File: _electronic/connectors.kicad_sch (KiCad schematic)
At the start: 7 parts

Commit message: BETA first upload
nothing major done here:
* updated KiCAD files to v9
* removed alternative 6v feed-in. The proposed buck converter is fine.
* added to all components LCSC component IDs. With this, exporting the project as gerber files also automatically creates correct BOM for JLCPCB manufacturing
*
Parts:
- J_HALL1, J_SERVO1: LCSC (none) -> C2937625
- J_LEDE1, J_LEDP1: LCSC (none) -> C492401
- J_OLED1: LCSC (none) -> C32713263
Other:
- title: E-TKT v1.0 -> E-TKT v2.0 BETA

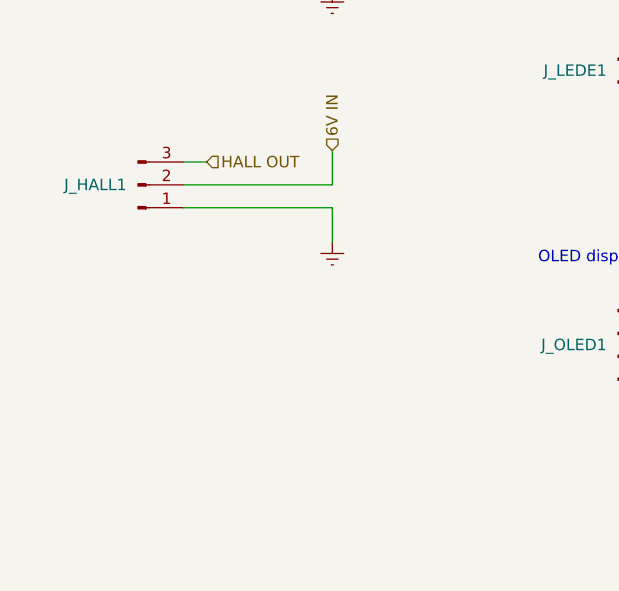
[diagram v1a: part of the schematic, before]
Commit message: Added endstop
added footprint for a microswitch with roller as enstop. updated the CAD correspondingly by adding M4 hole in the nema wheel hub for an M4 12mm/16mm set screw (the ones with a pointy end).
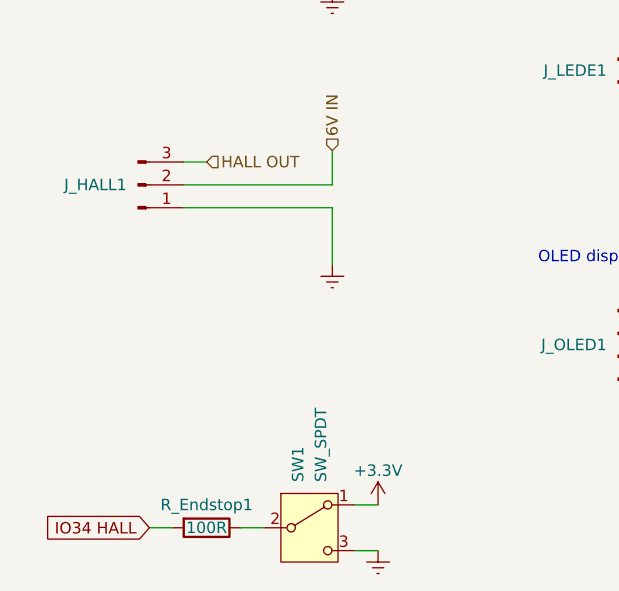
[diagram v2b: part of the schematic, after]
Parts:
- added R_Endstop1: 100R, Resistor_SMD:R_0603_1608Metric_Pad0.98x0.95mm_HandSolder, symbol Device:R
- added SW1: SW_SPDT, EASYEDA2KICAD:SW-TH_JL010, symbol Switch:SW_SPDT
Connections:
- net GNDREF: now also SW1.3 (C)
- new net: R_Endstop1.1, SW1.2 (B)
- new net +3.3V: SW1.1 (A)
- new net IO34 HALL: R_Endstop1.2

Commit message: sturdyfy E-TKT
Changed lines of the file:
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@@
 	(wire
 		(pts
-			(xy 135.89 154.94) (xy 138.43 154.94)
+			(xy 135.89 154.94) (xy 152.4 154.94)
 		)
 		(stroke
@@
 	(wire
 		(pts
-			(xy 135.89 149.86) (xy 138.43 149.86)
+			(xy 135.89 149.86) (xy 152.4 149.86)
 		)
 		(stroke
@@
 	(symbol
 		(lib_id "power:+3.3V")
-		(at 138.43 149.86 0)
+		(at 152.4 149.86 0)
 		(unit 1)
 		(exclude_from_sim no)
@@
 		(dnp no)
 		(property "Reference" "#PWR06"
-			(at 138.43 153.67 0)
+			(at 152.4 153.67 0)
 			(effects
 				(font
@@
 		)
 		(property "Value" "+3.3V"
-			(at 138.43 146.05 0)
+			(at 152.4 146.05 0)
 			(effects
 				(font
@@
 		)
 		(property "Footprint" ""
-			(at 138.43 149.86 0)
+			(at 152.4 149.86 0)
 			(effects
 				(font
@@
 		)
 		(property "Datasheet" ""
-			(at 138.43 149.86 0)
+			(at 152.4 149.86 0)
 			(effects
 				(font
@@
 		)
 		(property "Description" ""
-			(at 138.43 149.86 0)
+			(at 152.4 149.86 0)
 			(effects
 				(font
@@
 	(symbol
 		(lib_id "power:GNDREF")
-		(at 138.43 154.94 0)
+		(at 152.4 154.94 0)
 		(unit 1)
 		(exclude_from_sim no)
@@
 		(fields_autoplaced yes)
 		(property "Reference" "#PWR05"
-			(at 138.43 161.29 0)
+			(at 152.4 161.29 0)
 			(effects
 				(font
@@
 		)
 		(property "Value" "GNDREF"
-			(at 138.43 160.02 0)
+			(at 152.4 160.02 0)
 			(effects
 				(font
@@
 		)
 		(property "Footprint" ""
-			(at 138.43 154.94 0)
+			(at 152.4 154.94 0)
 			(effects
 				(font
@@
 		)
 		(property "Datasheet" ""
-			(at 138.43 154.94 0)
+			(at 152.4 154.94 0)
 			(effects
 				(font
@@
 		)
 		(property "Description" ""
-			(at 138.43 154.94 0)
-			(effects
-				(font
+			(at 152.4 154.94 0)
+			(effects
+				(font

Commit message: JLC export added, LCSC numbers updated
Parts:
- R_LEDE1, R_LEDP1: LCSC (none) -> C25190
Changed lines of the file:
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@@
+			)
+		)
+		(property "LCSC" "C25190"
+			(at 175.26 85.09 90)
+			(effects
+				(font
+					(size 1.27 1.27)
+				)
+				(hide yes)
 			)
 		)
@@
 			(effects
 				(font
+					(size 1.27 1.27)
+				)
+				(hide yes)
+			)
+		)
+		(property "LCSC" "C25190"
+			(at 175.26 100.33 90)
+			(effects
+				(font

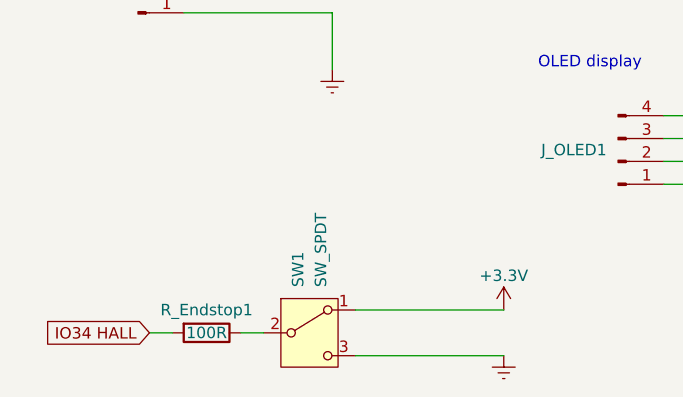
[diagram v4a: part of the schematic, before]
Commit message: Updated layout of schematic symbol's text
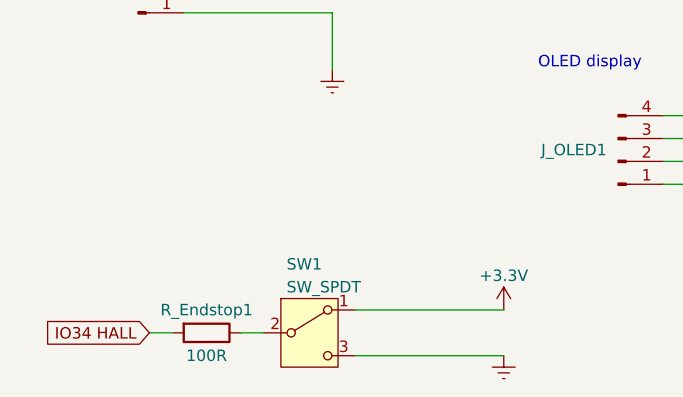
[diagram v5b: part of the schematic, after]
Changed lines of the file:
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@@
 		(on_board yes)
 		(dnp no)
-		(fields_autoplaced yes)
 		(property "Reference" "SW1"
-			(at 129.5399 147.32 90)
+			(at 128.27 144.78 0)
 			(effects
 				(font
@@
 		)
 		(property "Value" "SW_SPDT"
-			(at 132.0799 147.32 90)
+			(at 128.27 147.32 0)
 			(effects
 				(font
@@
 		)
 		(property "Value" "100R"
-			(at 119.38 152.4 90)
-			(effects
-				(font
+			(at 119.38 154.94 90)
+			(effects
+				(font
